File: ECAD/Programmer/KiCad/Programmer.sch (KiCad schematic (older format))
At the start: 51 parts, among them J1 USB_B_Micro, J2 ARM_SWD, J3 Prog, SW1 POWER VIA USB, U1 FT232RL, U2 STM32F105R8Tx, U3 74HCT245PWR, U4 74HCT245PWR, U5 TPS63030DSK

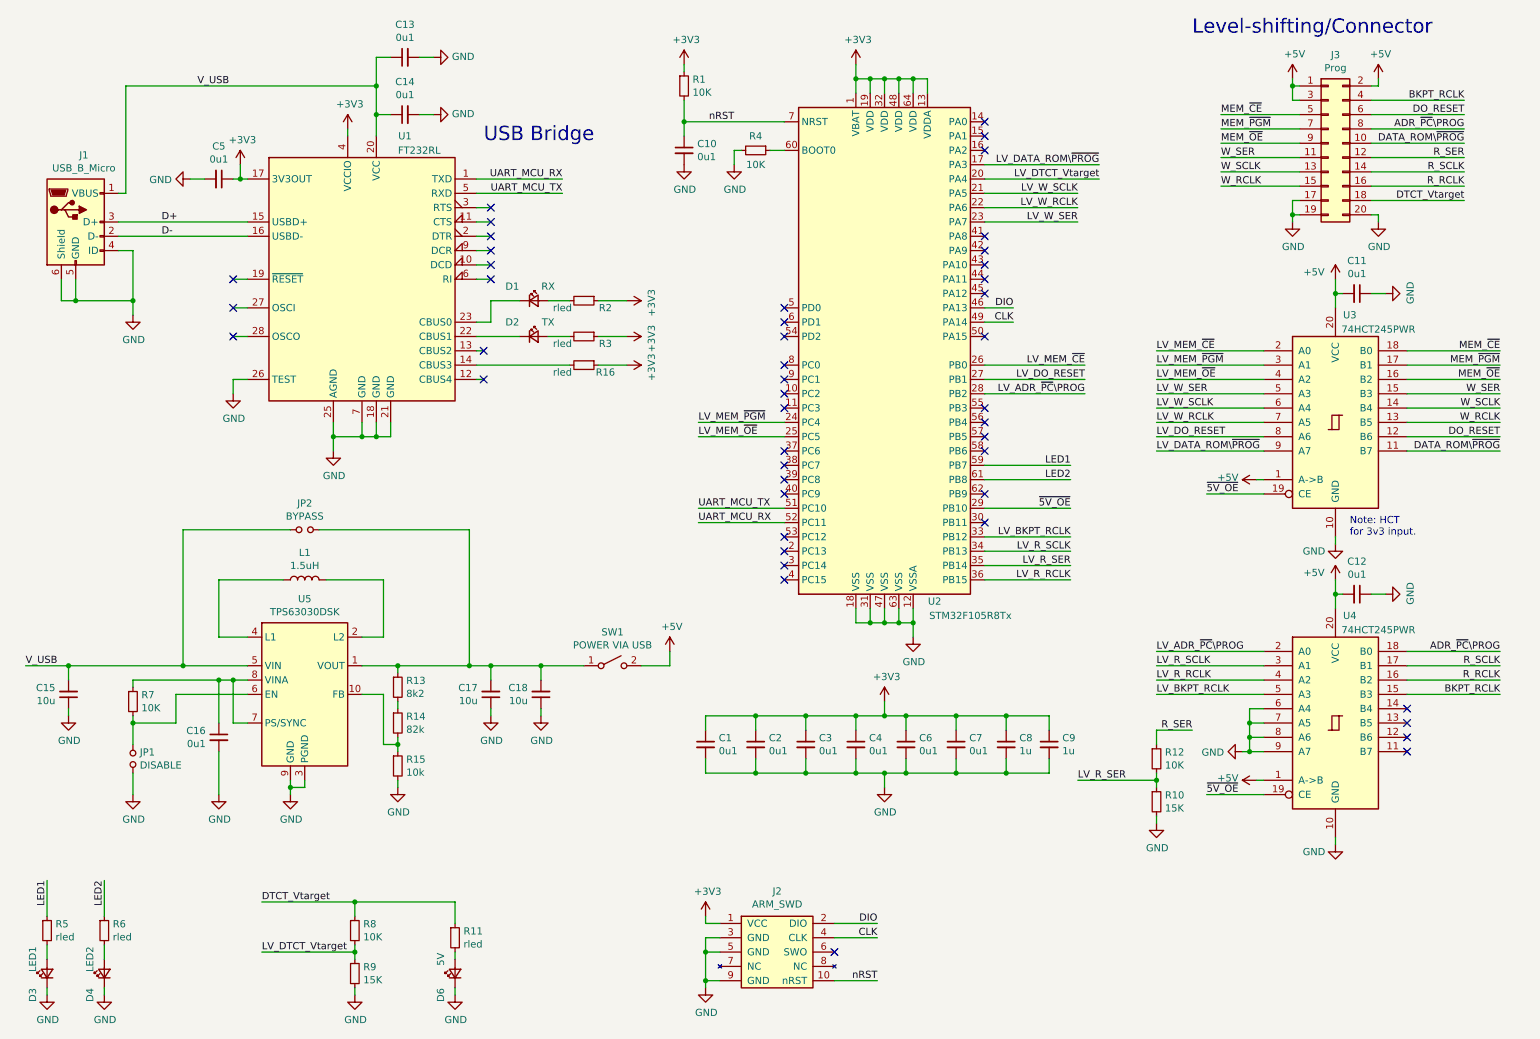
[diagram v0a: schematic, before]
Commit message: Changed Programmer to differnet STM32
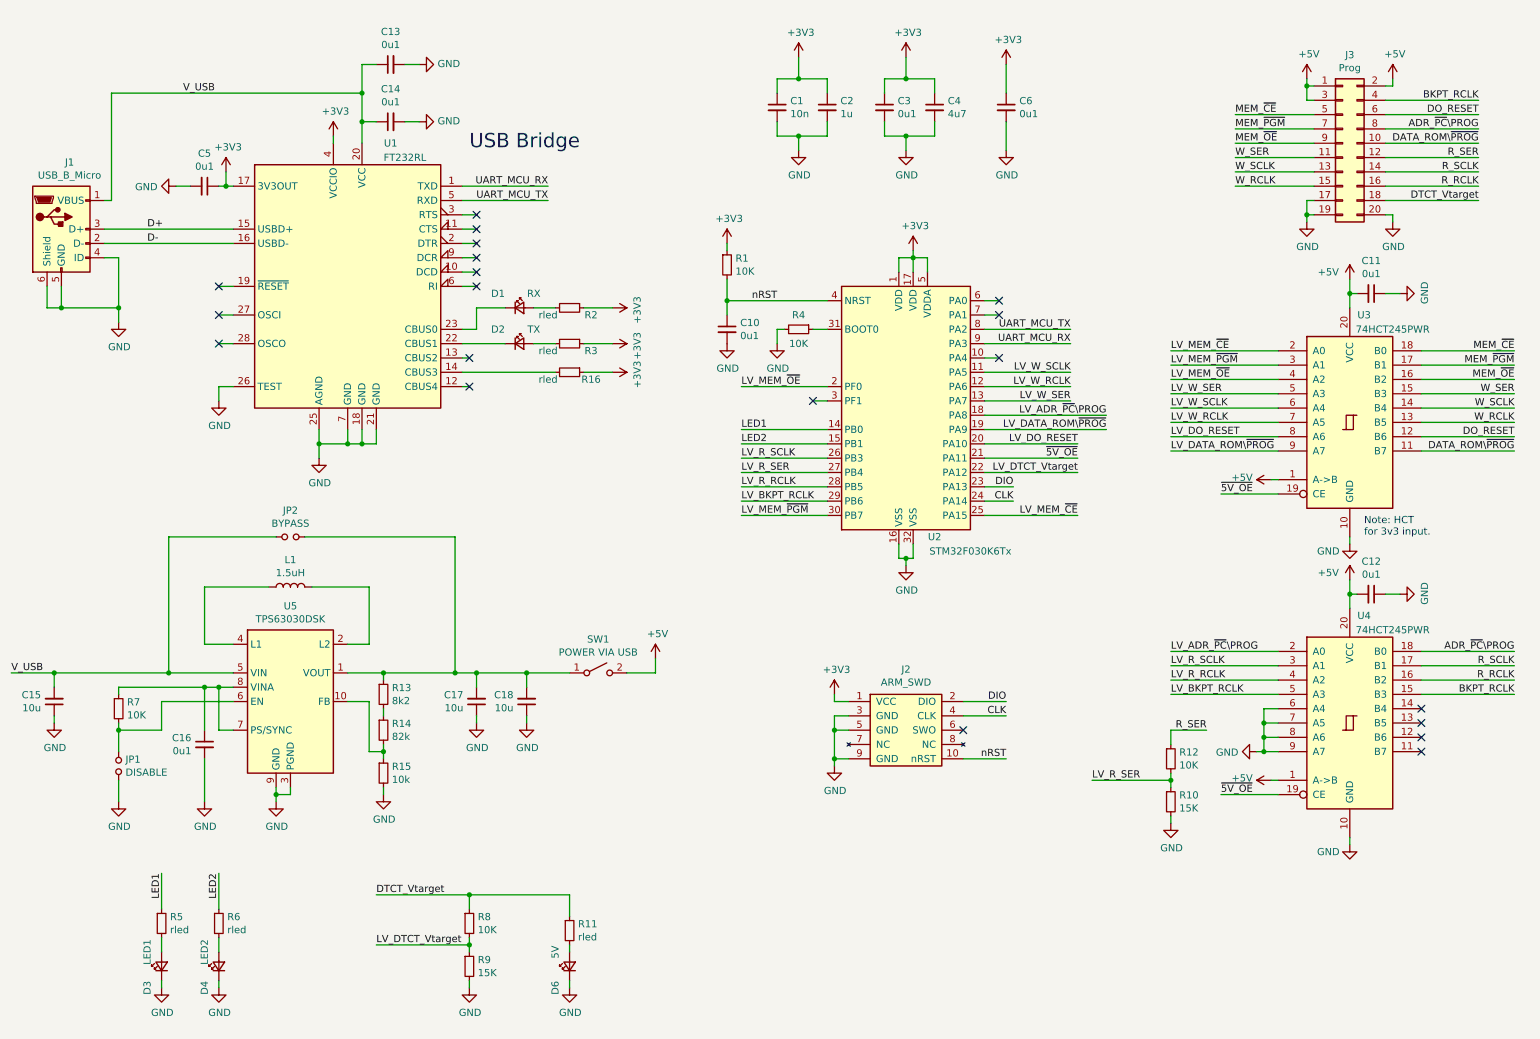
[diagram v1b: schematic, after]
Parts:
- removed C7: 0u1, Capacitor_SMD:C_0603_1608Metric, symbol Device:C_Small
- removed C8, C9: 1u, Capacitor_SMD:C_0603_1608Metric, symbol Device:C_Small
- removed U2: STM32F105R8Tx, Package_QFP:LQFP-64_10x10mm_P0.5mm, symbol MCU_ST_STM32F1:STM32F105R8Tx
- added U2: STM32F030K6Tx, Package_QFP:LQFP-32_7x7mm_P0.8mm, symbol MCU_ST_STM32F0:STM32F030K6Tx
- C1: value 0u1 -> 10n
- C2: value 0u1 -> 1u
- C4: value 0u1 -> 4u7
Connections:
- net +3V3: now also U2.1 (VDD), U2.17 (VDD), U2.5 (VDDA)
- net CLK: now also U2.24 (PA14)
- net DIO: now also U2.23 (PA13)
- net GND: now also U2.16 (VSS), U2.32 (VSS)
- net LED1: now also U2.14 (PB0)
- net LED2: now also U2.15 (PB1)
- net LV_ADR_~PC~\PROG: now also U2.18 (PA8)
- net LV_BKPT_RCLK: now also U2.29 (PB6)
- net LV_DATA_ROM\~PROG~: now also U2.19 (PA9)
- net LV_DO_RESET: now also U2.20 (PA10)
- net LV_DTCT_Vtarget: now also U2.22 (PA12)
- net LV_MEM_~CE: now also U2.25 (PA15)
- net LV_MEM_~OE: now also U2.2 (PF0)
- net LV_MEM_~PGM: now also U2.30 (PB7)
- net LV_R_RCLK: now also U2.28 (PB5)
- net LV_R_SCLK: now also U2.26 (PB3)
- net LV_R_SER: now also U2.27 (PB4)
- net LV_W_RCLK: now also U2.12 (PA6)
- net LV_W_SCLK: now also U2.11 (PA5)
- net LV_W_SER: now also U2.13 (PA7)
- net UART_MCU_RX: now also U2.9 (PA3)
- net UART_MCU_TX: now also U2.8 (PA2)
- net nRST: now also U2.4 (NRST)
- net ~5V_OE: now also U2.21 (PA11)
- net at R4.1: now also U2.31 (BOOT0)
- no-connect marks 46 -> 20
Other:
- note removed: "Level-shifting/Connector"
- moved on the sheet: C10, C11, C12, C13, C14, C15, C16, C17, C18, C5, D1, D2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

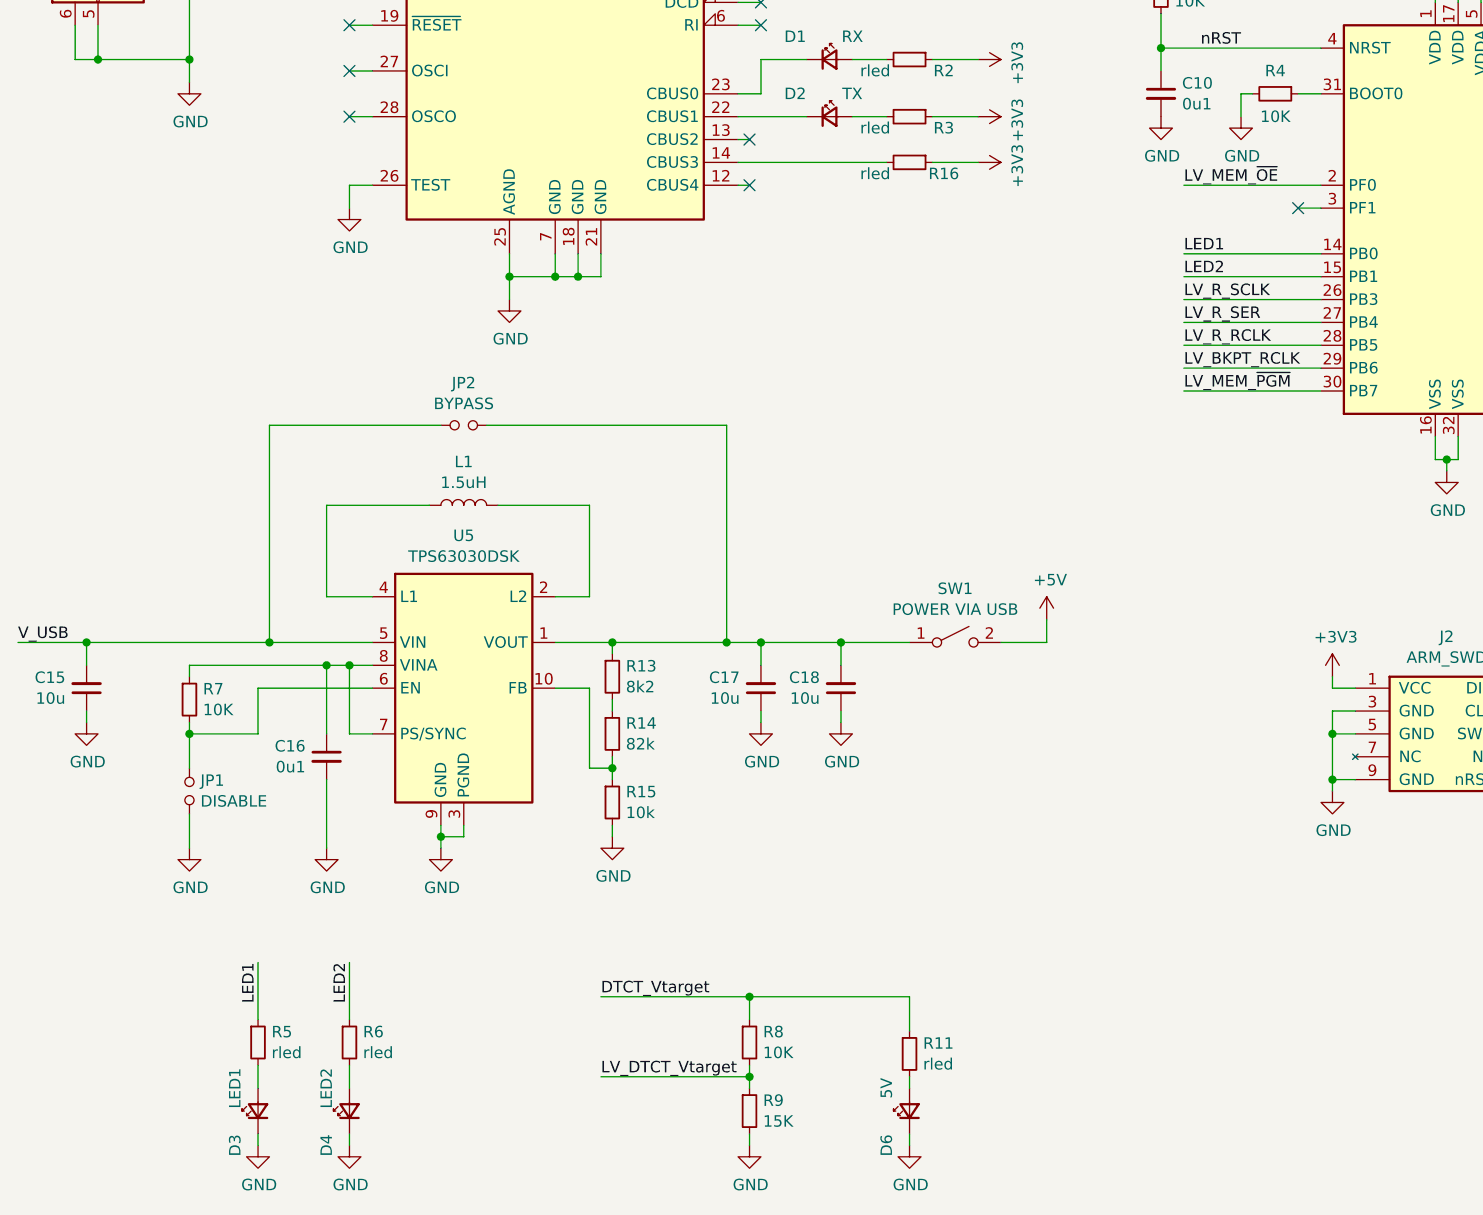
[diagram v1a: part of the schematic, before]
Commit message: First draft v1.0 schematic done, ready for verify
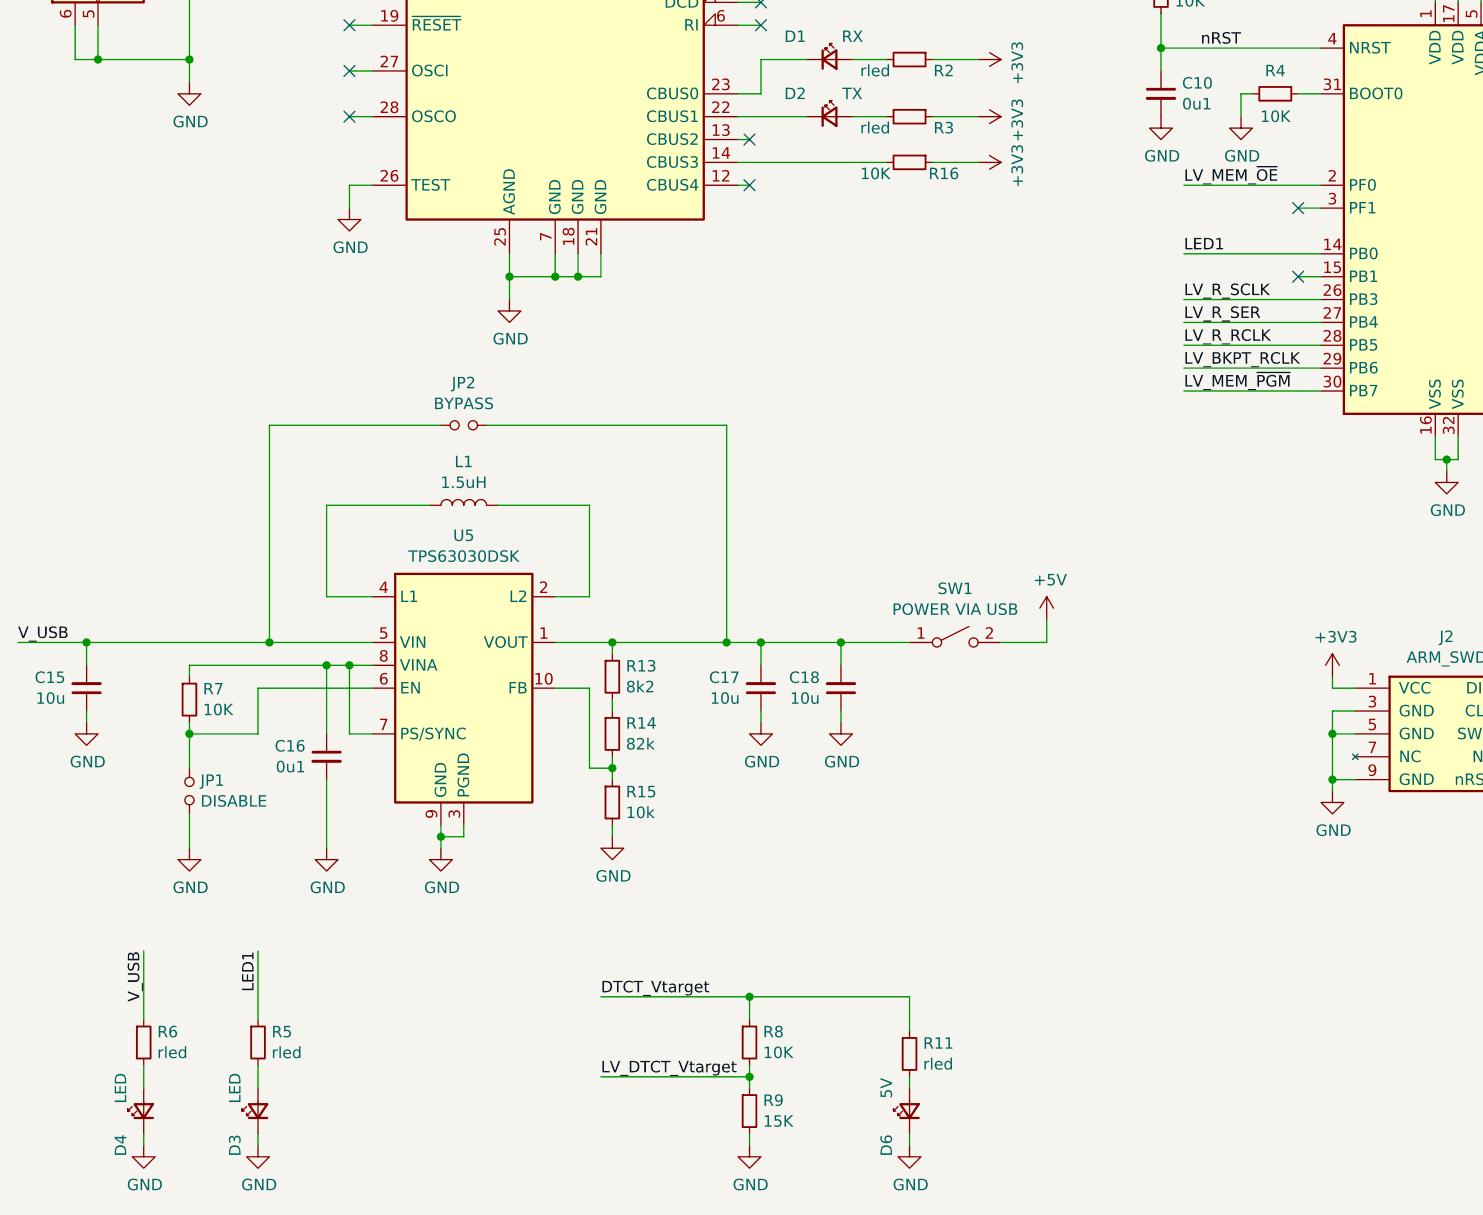
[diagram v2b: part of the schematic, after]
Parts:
- D3: value LED1 -> LED
- D4: value LED2 -> LED
- R16: value rled -> 10K
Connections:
- net V_USB: now also R6.1
- net LED2: no longer names the net of U2.15 (PB1)
- net LED2: no longer R6.1
- no-connect marks 20 -> 21
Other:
- moved on the sheet: D4, R6
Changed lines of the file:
@@
 Sheet 1 1
 Title "Programmer"
-Date "2021-03-30"
-Rev "v0.1"
+Date "2021-05-15"
+Rev "v1.0"
 Comp "Philipp Schilk"
 Comment1 ""
@@
 P 1650 7200
 F 0 "D3" H 1500 7300 50  0000 C CNN
-F 1 "LED1" H 1750 7300 50  0000 C CNN
+F 1 "LED" H 1750 7300 50  0000 C CNN
 F 2 "LED_SMD:LED_0603_1608Metric" V 1650 7200 50  0001 C CNN
 F 3 "~" V 1650 7200 50  0001 C CNN
@@
 L Device:R_Small R6
 U 1 1 6207A11B
-P 2050 6900
-F 0 "R6" H 2109 6946 50  0000 L CNN
-F 1 "rled" H 2109 6855 50  0000 L CNN
-F 2 "Resistor_SMD:R_0603_1608Metric" H 2050 6900 50  0001 C CNN
-F 3 "~" H 2050 6900 50  0001 C CNN
-	1    2050 6900
+P 1150 6900
+F 0 "R6" H 1209 6946 50  0000 L CNN
+F 1 "rled" H 1209 6855 50  0000 L CNN
+F 2 "Resistor_SMD:R_0603_1608Metric" H 1150 6900 50  0001 C CNN
+F 3 "~" H 1150 6900 50  0001 C CNN
+	1    1150 6900
 	1    0    0    -1
 $EndComp
@@
 L Device:LED_Small D4
 U 1 1 6207A121
-P 2050 7200
-F 0 "D4" H 1900 7300 50  0000 C CNN
-F 1 "LED2" H 2150 7300 50  0000 C CNN
-F 2 "LED_SMD:LED_0603_1608Metric" V 2050 7200 50  0001 C CNN
-F 3 "~" V 2050 7200 50  0001 C CNN
-	1    2050 7200
+P 1150 7200
+F 0 "D4" H 1000 7300 50  0000 C CNN
+F 1 "LED" H 1250 7300 50  0000 C CNN
+F 2 "LED_SMD:LED_0603_1608Metric" V 1150 7200 50  0001 C CNN
+F 3 "~" V 1150 7200 50  0001 C CNN
+	1    1150 7200
 	0    -1   -1   0
 $EndComp
 Wire Wire Line
-	2050 7100 2050 7000
+	1150 7100 1150 7000
 $Comp
 L power:GND #PWR0130
 U 1 1 6207A129
-P 2050 7350
-F 0 "#PWR0130" H 2050 7100 50  0001 C CNN
-F 1 "GND" H 2055 7177 50  0000 C CNN
-F 2 "" H 2050 7350 50  0001 C CNN
-F 3 "" H 2050 7350 50  0001 C CNN
-	1    2050 7350
-	1    0    0    -1
-$EndComp
-Wire Wire Line
-	2050 7350 2050 7300
-Wire Wire Line
-	1650 6550 1650 6800
-Wire Wire Line
-	2050 6550 2050 6800
-Text Label 1650 6550 3    50   ~ 0
+P 1150 7350
+F 0 "#PWR0130" H 1150 7100 50  0001 C CNN
+F 1 "GND" H 1155 7177 50  0000 C CNN
+F 2 "" H 1150 7350 50  0001 C CNN
+F 3 "" H 1150 7350 50  0001 C CNN
+	1    1150 7350
+	1    0    0    -1
+$EndComp
+Wire Wire Line
+	1150 7350 1150 7300
+Wire Wire Line
+	1650 6500 1650 6800
+Wire Wire Line
+	1150 6500 1150 6800
+Text Label 1650 6500 3    50   ~ 0
 LED1
-Text Label 2050 6550 3    50   ~ 0
-LED2
 Wire Wire Line
 	5600 2550 6300 2550
@@
 P 4500 3050
 F 0 "R16" V 4550 3200 50  0000 C CNN
-F 1 "rled" V 4550 2900 50  0000 C CNN
+F 1 "10K" V 4550 2900 50  0000 C CNN
 F 2 "Resistor_SMD:R_0603_1608Metric" H 4500 3050 50  0001 C CNN
 F 3 "~" H 4500 3050 50  0001 C CNN
@@
 Text Label 5700 3450 0    50   ~ 0
 LED1
-Text Label 5700 3550 0    50   ~ 0
-LED2
 Text Label 8250 3450 2    50   ~ 0
 LV_DATA_ROM\~PROG~
@@
 Wire Wire Line
 	6300 3450 5700 3450
-Wire Wire Line
-	6300 3550 5700 3550
 Text Label 5700 4050 0    50   ~ 0
 LV_MEM_~PGM
@@
 	1    0    0    -1
 $EndComp
+Wire Wire Line
+	6200 3550 6300 3550
+NoConn ~ 6200 3550
+Text Label 1150 6500 3    50   ~ 0
+V_USB
 $EndSCHEMATC
